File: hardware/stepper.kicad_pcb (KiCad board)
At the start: 4 copper layers, 40 x 40 mm, 108 parts, among them J1 DRILL, J2 DRILL, J3 DRILL, J4 DRILL, J5 USB-MINI-B-SMD, J6 STACK-UP-HIGH, J7 STACK-DOWN, J8 STACK-UP-HIGH, J9 STACK-DOWN, P1 black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

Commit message: Add missing 3d information
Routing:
- net 3V3: track 244.1 -> 285.2 mm, vias 19 -> 20
- net GND: track 373.7 -> 332.6 mm, vias 40 -> 39

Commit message: Add heatsink and new switches to 3d model
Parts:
- added REF**: heatsink, kicad-libraries:heatsink, F.Cu at (153.2, 93.6)
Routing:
- net GND: track 332.6 -> 319.3 mm, vias 39 -> 38
- net 3V3: track 285.2 -> 298.5 mm, vias 20 -> 21

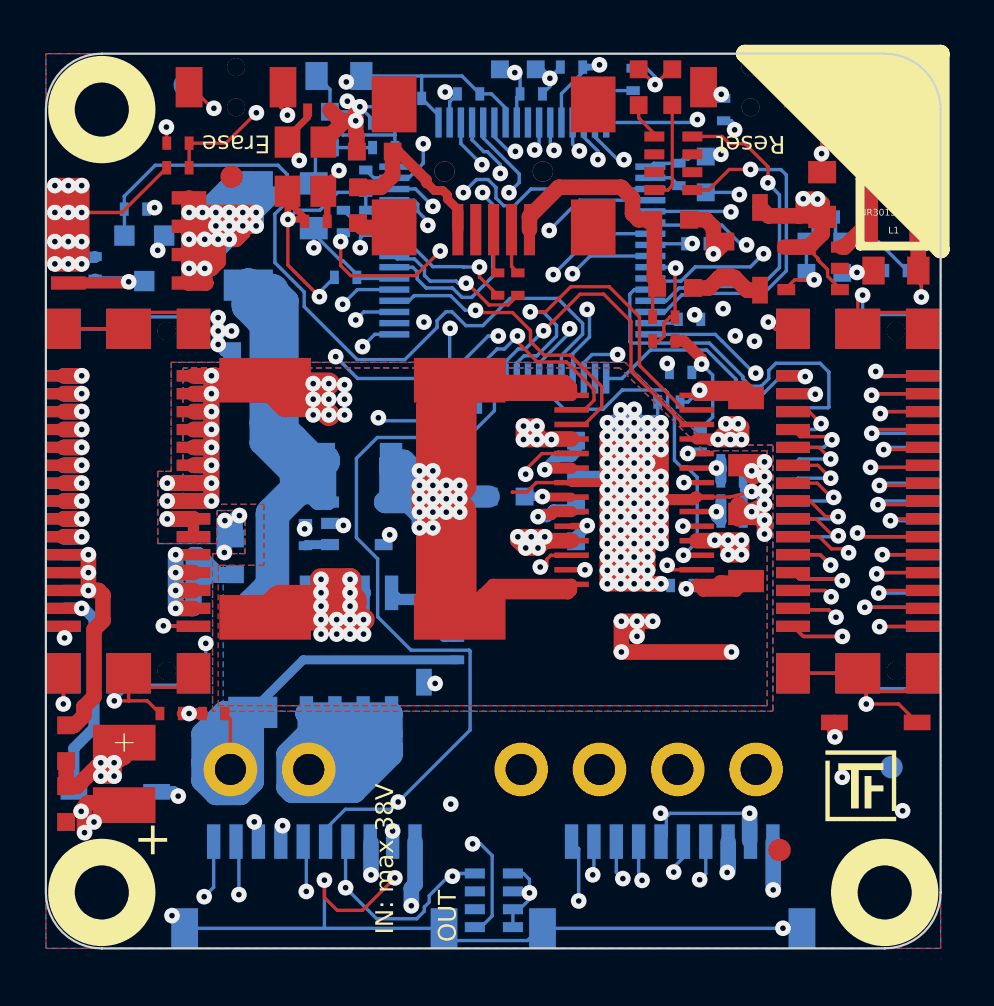
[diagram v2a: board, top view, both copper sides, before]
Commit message: Fix orientation of diodes
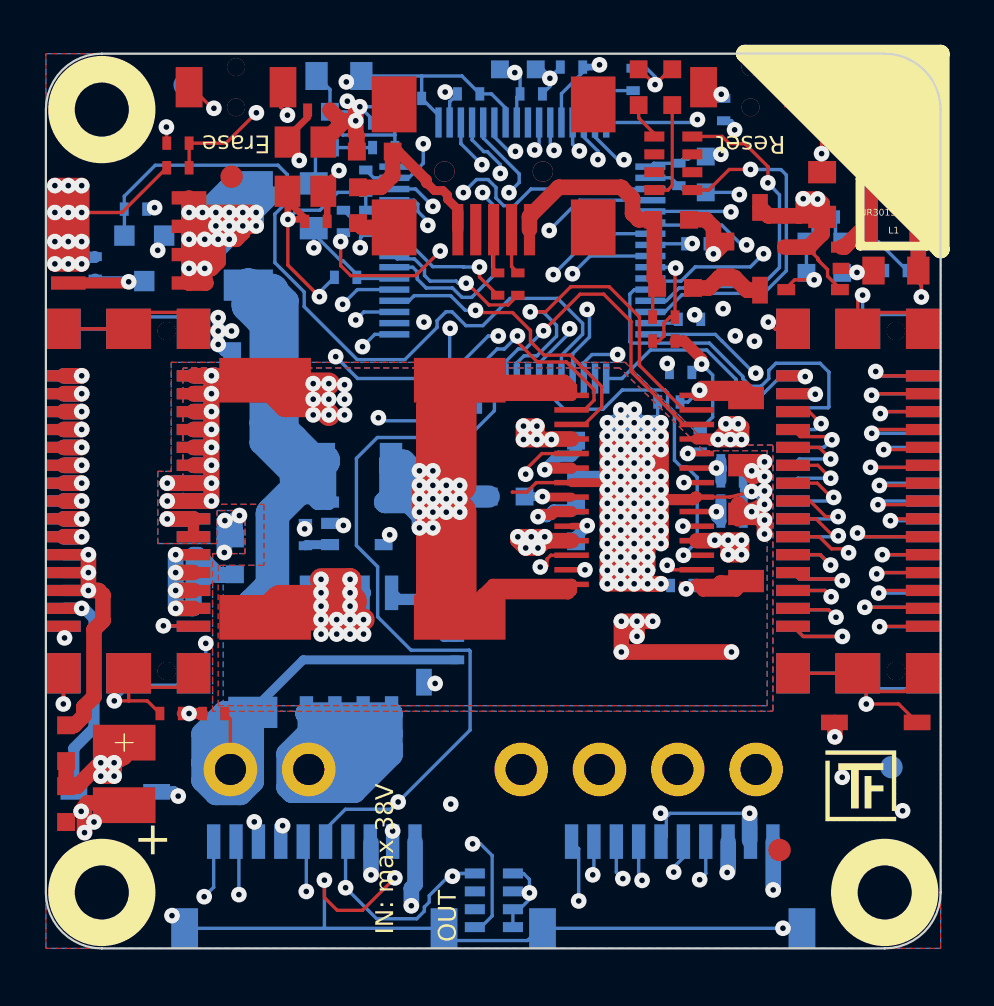
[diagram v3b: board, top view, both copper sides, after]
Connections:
- D3 pad 1: Net-(D3-Pad1) -> STACK-PGND
- D3 pad 2: STACK-PGND -> Net-(D3-Pad2)
- D8 pad 1: 3V3 -> GND
- D8 pad 2: GND -> 3V3
- Q1 pad D: N-000112 -> Net-(P1-Pad2)
- Q1 pad G: N-000103 -> Net-(D3-Pad2)
- Q2 pad D: N-000110 -> Net-(D4-Pad1)
- Q2 pad G: N-000120 -> Net-(Q2-PadG)
- Q3 pad D: N-000120 -> Net-(Q2-PadG)
- R8 pad 1: Net-(R8-Pad1) -> Net-(Q2-PadG)
- R9 pad 2: Net-(D3-Pad1) -> Net-(D3-Pad2)
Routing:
- net GND: track 319.3 -> 386.5 mm, vias 38 -> 43
- net 3V3: track 298.5 -> 231.3 mm, vias 21 -> 16
- net Net-(D4-Pad1): track 6.34 -> 38.5 mm, vias 0 -> 16
- net N-000110: track 32.2 -> 0.00 mm, vias 16 -> 0
- net Net-(P1-Pad2): track 10.2 -> 30.1 mm
- net N-000112: track 19.9 -> 0.00 mm
- net Net-(Q2-PadG): track 0.00 -> 5.00 mm, vias 0 -> 1
- net Net-(D3-Pad2): track 0.00 -> 4.24 mm
- net N-000120: track 3.43 -> 0.00 mm, vias 1 -> 0
- net N-000103: track 1.57 -> 0.00 mm
- net Net-(R8-Pad1): track 1.57 -> 0.00 mm
- net STACK-PGND: track 245.8 -> 244.2 mm
- net Net-(D3-Pad1): track 1.13 -> 0.00 mm
